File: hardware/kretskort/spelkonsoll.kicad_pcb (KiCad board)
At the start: 2 copper layers, 176.6 x 56.6 mm, 18 parts, among them SW1 SW_Push, SW10 SW_Push, SW11 SW_Push, SW12 SW_Push, SW2 SW_Push, SW3 SW_Push, SW4 SW_Push, SW5 SW_Push, SW6 SW_Push, SW7 SW_Push, SW8 SW_Push, SW9 SW_Push, U2 ESP32-DEVKITC-32D, U3 ILI9488

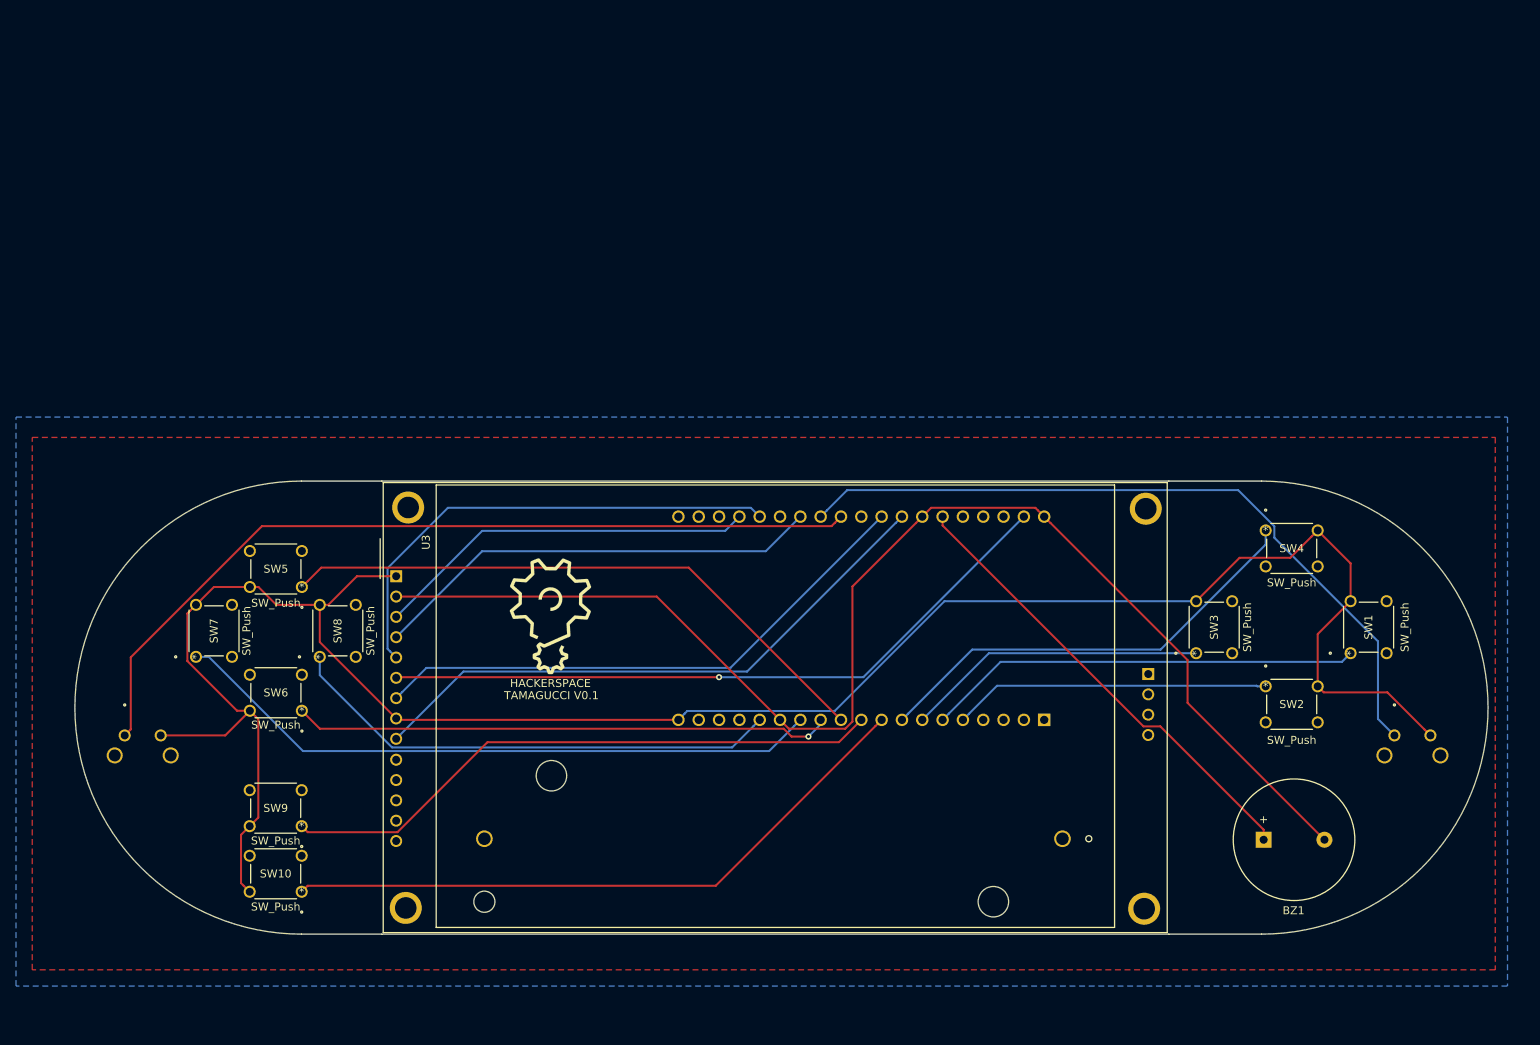
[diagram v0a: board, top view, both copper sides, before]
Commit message: started on v0.2 moved resistors and added silkscreen for inputs on the ESP32
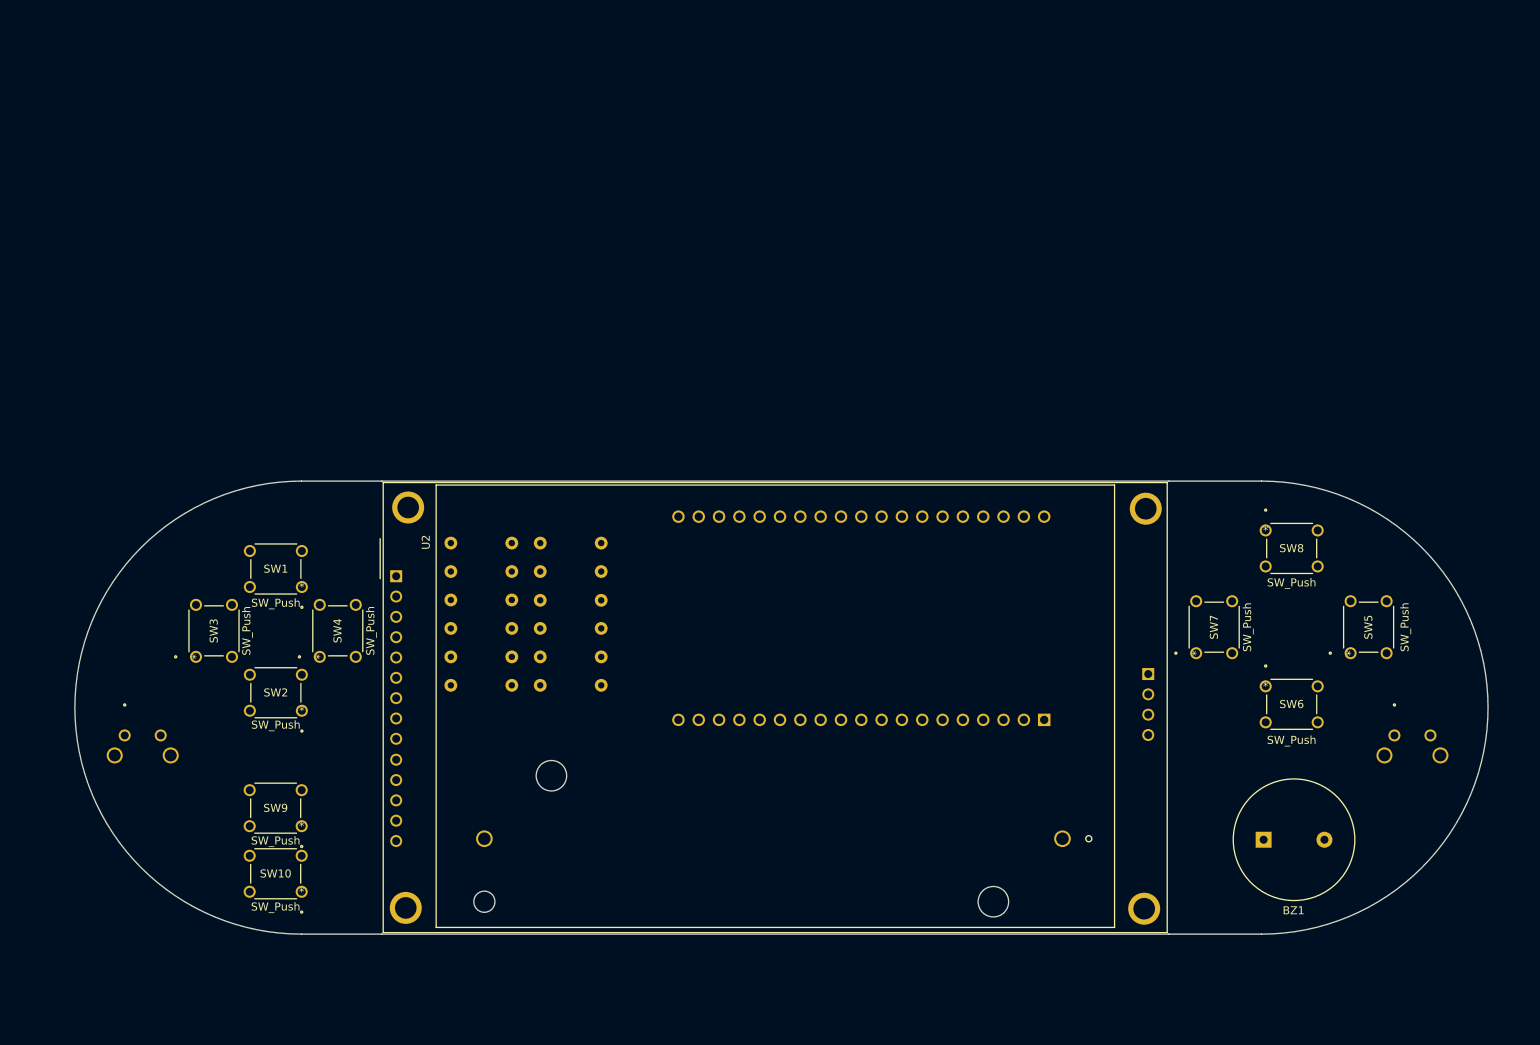
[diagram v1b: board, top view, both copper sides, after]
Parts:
- removed the G*** at (117.3, 86.1)
- removed U3: ILI9488, ESP32-DEVKITC-32D:ILI9488
- added R1: 10K, Resistor_THT:R_Axial_DIN0207_L6.3mm_D2.5mm_P7.62mm_Horizontal, B.Cu at (104.9, 94.7)
- added R10: 10K, Resistor_THT:R_Axial_DIN0207_L6.3mm_D2.5mm_P7.62mm_Horizontal, B.Cu at (116.1, 84.1)
- added R11: 10K, Resistor_THT:R_Axial_DIN0207_L6.3mm_D2.5mm_P7.62mm_Horizontal, B.Cu at (116.1, 80.5)
- added R12: 10K, Resistor_THT:R_Axial_DIN0207_L6.3mm_D2.5mm_P7.62mm_Horizontal, B.Cu at (116.1, 77.0)
- added R2: 10K, Resistor_THT:R_Axial_DIN0207_L6.3mm_D2.5mm_P7.62mm_Horizontal, B.Cu at (104.9, 91.2)
- added R3: 10K, Resistor_THT:R_Axial_DIN0207_L6.3mm_D2.5mm_P7.62mm_Horizontal, B.Cu at (104.9, 87.6)
- added R4: 10K, Resistor_THT:R_Axial_DIN0207_L6.3mm_D2.5mm_P7.62mm_Horizontal, B.Cu at (104.9, 84.1)
- added R5: 10K, Resistor_THT:R_Axial_DIN0207_L6.3mm_D2.5mm_P7.62mm_Horizontal, B.Cu at (104.9, 80.5)
- added R6: 10K, Resistor_THT:R_Axial_DIN0207_L6.3mm_D2.5mm_P7.62mm_Horizontal, B.Cu at (104.9, 77.0)
- added R7: 10K, Resistor_THT:R_Axial_DIN0207_L6.3mm_D2.5mm_P7.62mm_Horizontal, B.Cu at (116.1, 94.7)
- added R8: 10K, Resistor_THT:R_Axial_DIN0207_L6.3mm_D2.5mm_P7.62mm_Horizontal, B.Cu at (116.1, 91.2)
- added R9: 10K, Resistor_THT:R_Axial_DIN0207_L6.3mm_D2.5mm_P7.62mm_Horizontal, B.Cu at (116.1, 87.6)
- added U1: ESP32-DEVKITC-32D, ESP32-DEVKITC-32D:MODULE_ESP32-DEVKITC-32D, B.Cu at (159.3, 86.4)
- U2: value ESP32-DEVKITC-32D -> ILI9488; footprint ESP32-DEVKITC-32D:MODULE_ESP32-DEVKITC-32D -> ESP32-DEVKITC-32D:ILI9488; moved to F.Cu
- moved G*** 83.9 mm to (197.9, 109.6)
- moved U2 22.2 mm to (150.1, 106.6), turned to 0 degrees
- renumbered SW5 to SW1, SW6 to SW2, SW7 to SW3, SW8 to SW4, SW1 to SW5, SW2 to SW6, SW3 to SW7, SW4 to SW8
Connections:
- U2 pad 1: Net-(U2-Pad1) -> +5V
- U2 pad 10: BTN_START -> Net-(U2-Pad10)
- U2 pad 11: BTN_DP_UP -> Net-(U2-Pad11)
- U2 pad 12: BTN_DP_DOWN -> Net-(U2-Pad12)
- U2 pad 13: BTN_DP_LEFT -> Net-(U2-Pad13)
- U2 pad 14: GND -> Net-(U2-Pad14)
- U2 pad 15: BTN_DP_RIGHT -> Net-(U2-Pad15)
- U2 pad 2: Net-(U2-Pad2) -> GND
- U2 pad 3: Net-(U2-Pad3) -> CS
- U2 pad 4: Net-(U2-Pad4) -> RESET
- U2 pad 5: BTN_B -> DC\RS
- U2 pad 6: BTN_A -> MOSI
- U2 pad 7: BTN_X -> SCK
- U2 pad 8: BTN_Y -> +5V
- U2 pad 9: BTN_SELECT -> MISO
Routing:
- net +5V: track 266.0 -> 0.00 mm
- net GND: track 164.6 -> 0.11 mm
- net BTN_BUMPER_L: track 106.1 -> 0.00 mm
- net BTN_BUMPER_R: track 92.3 -> 0.00 mm
- net MOSI: track 86.8 -> 0.11 mm, vias 1 -> 0
- net BTN_DP_LEFT: track 82.0 -> 0.00 mm
- net BTN_SELECT: track 81.4 -> 0.00 mm
- net BTN_DP_UP: track 76.3 -> 0.00 mm
- net BTN_START: track 76.1 -> 0.00 mm
- net MISO: track 74.7 -> 0.00 mm
- net SCK: track 70.1 -> 0.00 mm
- net BTN_DP_DOWN: track 67.4 -> 0.00 mm, vias 1 -> 0
- net BTN_DP_RIGHT: track 62.4 -> 0.00 mm
- net DC\RS: track 61.7 -> 0.00 mm
- net BUZZER: track 58.2 -> 0.00 mm
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- removed copper zone on B.Cu, net GND
- removed copper zone on F.Cu, net GND
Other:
- board text added: "TAMAGUCCI V0.2"
- board text removed: "TAMAGUCCI V0.1"

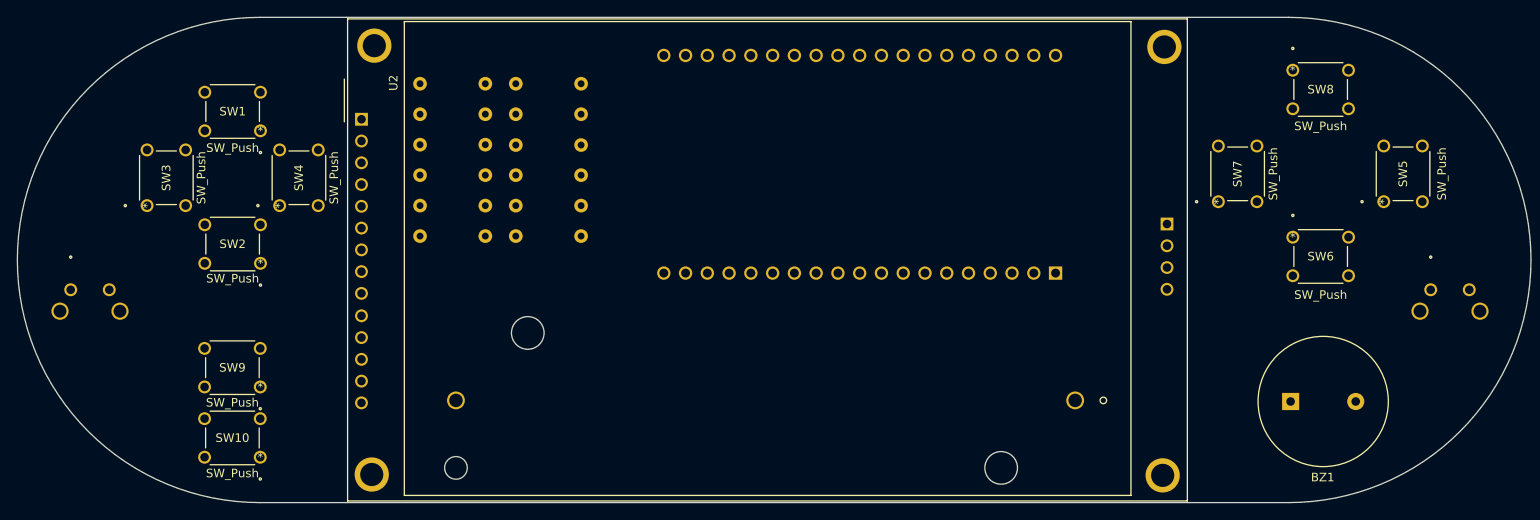
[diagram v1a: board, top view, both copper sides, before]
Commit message: Added schema from v0.1, deleted buttons
Moved resistors and deleted start, select, and shoulder buttons
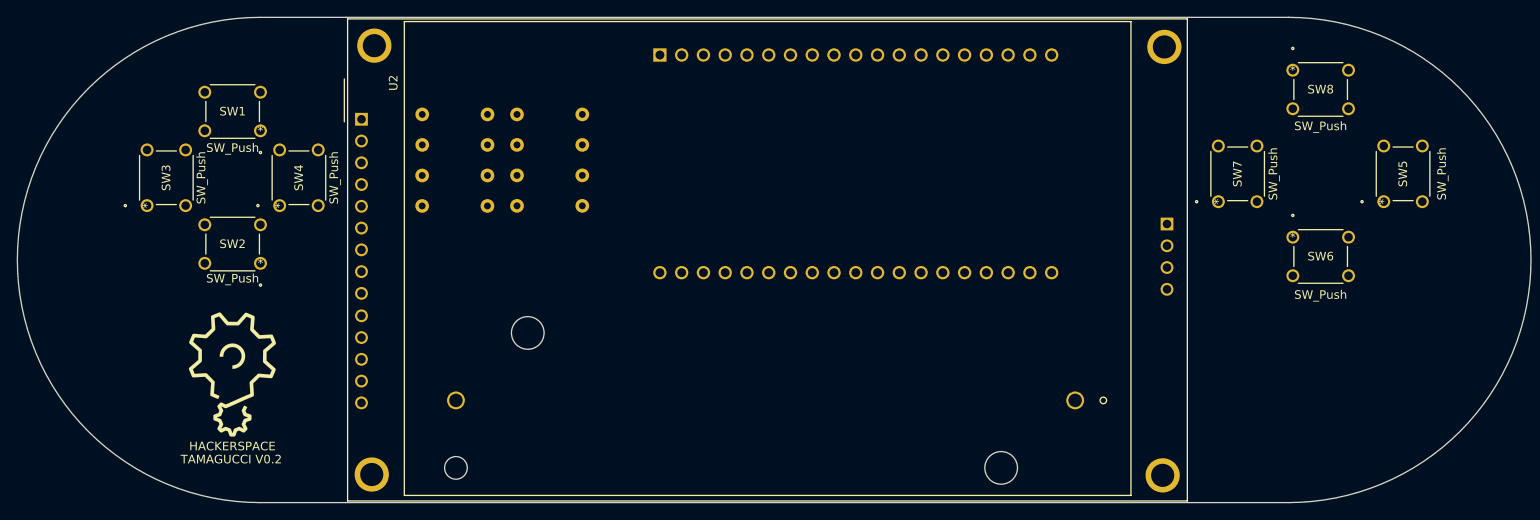
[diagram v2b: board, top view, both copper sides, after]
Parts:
- removed BZ1: Buzzer, Buzzer_Beeper:Buzzer_15x7.5RM7.6
- removed R10, R11, R12, R9: 10K, Resistor_THT:R_Axial_DIN0207_L6.3mm_D2.5mm_P7.62mm_Horizontal
- removed SW10, SW9: SW_Push, footprints:B3F1052
- removed SW11, SW12: SW_Push, footprints:B3F-3152
- added G***: LOGO, kretskort:hs_logo, B.Cu at (206.1, 110.5)
- G***: moved to F.Cu
- moved G*** 114.9 mm to (83.0, 110.9), turned to 0 degrees
- moved R1 23.7 mm to (123.8, 80.5), turned to 180 degrees
- moved R4 20.2 mm to (123.8, 91.2), turned to 180 degrees
- moved R2 20.2 mm to (123.8, 84.1), turned to 180 degrees
- moved R3 18.9 mm to (123.8, 87.7), turned to 180 degrees
- moved R6 10.6 mm to (112.8, 84.1), turned to 180 degrees
- moved R5 7.87 mm to (112.8, 80.5), turned to 180 degrees
- moved R7 7.81 mm to (112.8, 87.7), turned to 180 degrees
- moved U1 6.65 mm to (152.7, 86.3), turned to 270 degrees
- moved R8 3.31 mm to (112.8, 91.2), turned to 180 degrees
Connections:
- U1 pad 10: BTN_START -> BTN_DP_UP
- U1 pad 11: BTN_DP_UP -> BTN_DP_DOWN
- U1 pad 12: BTN_DP_DOWN -> BTN_DP_LEFT
- U1 pad 13: BTN_DP_LEFT -> Net-(U1-Pad13)
- U1 pad 25: BUZZER -> BTN_A
- U1 pad 30: BTN_BUMPER_L -> DC\RS
- U1 pad 31: BTN_BUMPER_R -> CS
- U1 pad 34: DC\RS -> Net-(U1-Pad34)
- U1 pad 35: CS -> Net-(U1-Pad35)
- U1 pad 5: BTN_B -> Net-(U1-Pad5)
- U1 pad 6: BTN_A -> Net-(U1-Pad6)
- U1 pad 7: BTN_X -> BTN_B
- U1 pad 8: BTN_Y -> BTN_X
- U1 pad 9: BTN_SELECT -> BTN_Y

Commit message: update KiCad files
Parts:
- removed BT1: Battery_Cell, footprints:18650holder
- added SW1: B3F-1052, footprints:Button, F.Cu at (110.3, 46.6)
- added SW2: B3F-1052, footprints:Button, F.Cu at (202.2, 13.8)
- added SW3: B3F-1052, footprints:Button, F.Cu at (126.6, 46.6)
- added SW4: B3F-1052, footprints:Button, F.Cu at (202.2, 30.3)
- added SW5: B3F-1052, footprints:Button, F.Cu at (143.0, 46.6)
- added SW6: B3F-1052, footprints:Button, F.Cu at (159.3, 46.6)
- added SW7: B3F-1052, footprints:Button, F.Cu at (175.6, 46.6)
- added SW8: B3F-1052, footprints:Button, F.Cu at (192.0, 46.8)
- added U3: 1043, footprints:18650holder, F.Cu at (179.8, 113.8)
- moved R1 7.63 mm to (116.2, 80.5), turned to 0 degrees
